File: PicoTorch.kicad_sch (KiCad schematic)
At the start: 44 parts, among them J1 Screw_Terminal_01x02, M1 Fan, M2 Fan, M3 Fan, M4 Fan, Q1 IRLB8721, Q2 IRLB8721, Q3 IRLB8721, Q4 IRLB8721, T1R1 4.7k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

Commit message: changes
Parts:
- D1, D3, D5, D7: footprint LED_THT:LED_D5.0mm_IRGrey -> LED_THT:LED_D1.8mm_W3.3mm_H2.4mm; LCSC C84256 -> (none); MPN 17-215SURC/S530-A2/TR8 -> (none); SKU 304090046 -> (none)
- J1, M4: footprint TerminalBlock_Philmore:TerminalBlock_Philmore_TB132_1x02_P5.00mm_Horizontal -> TerminalBlock_Phoenix:TerminalBlock_Phoenix_MKDS-1,5-2_1x02_P5.00mm_Horizontal
- R1, R10, R11, R12, R2, R3, R4, R5, R6, R7, R8, R9, T1R1, T1R2, T1R3, T1R4: footprint Resistor_THT:R_Axial_DIN0204_L3.6mm_D1.6mm_P5.08mm_Horizontal -> Resistor_THT:R_Axial_DIN0207_L6.3mm_D2.5mm_P2.54mm_Vertical
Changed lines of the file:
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@@
       (effects (font (size 1.27 1.27)) (justify right))
     )
-    (property "Footprint" "LED_THT:LED_D5.0mm_IRGrey" (at 74.93 33.909 0)
-      (effects (font (size 1.27 1.27)) hide)
-    )
-    (property "Datasheet" "https://www.prtice.info/IMG/pdf/CQY99.pdf" (at 70.485 32.639 0)
-      (effects (font (size 1.27 1.27)) hide)
-    )
-    (property "LCSC" "C84256" (at 70.485 33.909 90)
-      (effects (font (size 1.27 1.27)) hide)
-    )
-    (property "MPN" "17-215SURC/S530-A2/TR8 " (at 70.0532 34.8996 0)
-      (effects (font (size 1.27 1.27)) hide)
-    )
-    (property "SKU" "304090046" (at 70.0532 34.8996 0)
+    (property "Footprint" "LED_THT:LED_D1.8mm_W3.3mm_H2.4mm" (at 74.93 33.909 0)
+      (effects (font (size 1.27 1.27)) hide)
+    )
+    (property "Datasheet" "" (at 70.485 32.639 0)
       (effects (font (size 1.27 1.27)) hide)
     )
@@
       (effects (font (size 1.27 1.27)) (justify right))
     )
-    (property "Footprint" "Resistor_THT:R_Axial_DIN0204_L3.6mm_D1.6mm_P5.08mm_Horizontal" (at 130.683 37.084 0)
+    (property "Footprint" "Resistor_THT:R_Axial_DIN0207_L6.3mm_D2.5mm_P2.54mm_Vertical" (at 130.683 37.084 0)
       (effects (font (size 1.27 1.27)) hide)
     )
@@
       (effects (font (size 1.27 1.27)))
     )
-    (property "Footprint" "TerminalBlock_Philmore:TerminalBlock_Philmore_TB132_1x02_P5.00mm_Horizontal" (at 71.12 103.505 0)
+    (property "Footprint" "TerminalBlock_Phoenix:TerminalBlock_Phoenix_MKDS-1,5-2_1x02_P5.00mm_Horizontal" (at 71.12 103.505 0)
       (effects (font (size 1.27 1.27)) hide)
     )
@@
       (effects (font (size 1.27 1.27)) (justify right))
     )
-    (property "Footprint" "Resistor_THT:R_Axial_DIN0204_L3.6mm_D1.6mm_P5.08mm_Horizontal" (at 76.962 77.47 0)
+    (property "Footprint" "Resistor_THT:R_Axial_DIN0207_L6.3mm_D2.5mm_P2.54mm_Vertical" (at 76.962 77.47 0)
       (effects (font (size 1.27 1.27)) hide)
     )
@@
       (effects (font (size 1.27 1.27)) (justify right))
     )
-    (property "Footprint" "LED_THT:LED_D5.0mm_IRGrey" (at 116.586 34.163 0)
-      (effects (font (size 1.27 1.27)) hide)
-    )
-    (property "Datasheet" "https://www.prtice.info/IMG/pdf/CQY99.pdf" (at 112.141 32.893 0)
-      (effects (font (size 1.27 1.27)) hide)
-    )
-    (property "LCSC" "C84256" (at 112.141 34.163 90)
-      (effects (font (size 1.27 1.27)) hide)
-    )
-    (property "MPN" "17-215SURC/S530-A2/TR8 " (at 111.7092 35.1536 0)
-      (effects (font (size 1.27 1.27)) hide)
-    )
-    (property "SKU" "304090046" (at 111.7092 35.1536 0)
+    (property "Footprint" "LED_THT:LED_D1.8mm_W3.3mm_H2.4mm" (at 116.586 34.163 0)
+      (effects (font (size 1.27 1.27)) hide)
+    )
+    (property "Datasheet" "" (at 112.141 32.893 0)
       (effects (font (size 1.27 1.27)) hide)
     )
@@
       (effects (font (size 1.27 1.27)) (justify right))
     )
-    (property "Footprint" "Resistor_THT:R_Axial_DIN0204_L3.6mm_D1.6mm_P5.08mm_Horizontal" (at 77.47 41.148 0)
+    (property "Footprint" "Resistor_THT:R_Axial_DIN0207_L6.3mm_D2.5mm_P2.54mm_Vertical" (at 77.47 41.148 0)
       (effects (font (size 1.27 1.27)) hide)
     )
@@
       (effects (font (size 1.27 1.27)))
     )
-    (property "Footprint" "Resistor_THT:R_Axial_DIN0204_L3.6mm_D1.6mm_P5.08mm_Horizontal" (at 245.745 34.925 0)
+    (property "Footprint" "Resistor_THT:R_Axial_DIN0207_L6.3mm_D2.5mm_P2.54mm_Vertical" (at 245.745 34.925 0)
       (effects (font (size 1.27 1.27)) hide)
     )
@@
       (effects (font (size 1.27 1.27)) (justify right))
     )
-    (property "Footprint" "LED_THT:LED_D5.0mm_IRGrey" (at 116.078 70.485 0)
-      (effects (font (size 1.27 1.27)) hide)
-    )
-    (property "Datasheet" "https://www.prtice.info/IMG/pdf/CQY99.pdf" (at 111.633 69.215 0)
-      (effects (font (size 1.27 1.27)) hide)
-    )
-    (property "LCSC" "C84256" (at 111.633 70.485 90)
-      (effects (font (size 1.27 1.27)) hide)
-    )
-    (property "MPN" "17-215SURC/S530-A2/TR8 " (at 111.2012 71.4756 0)
-      (effects (font (size 1.27 1.27)) hide)
-    )
-    (property "SKU" "304090046" (at 111.2012 71.4756 0)
+    (property "Footprint" "LED_THT:LED_D1.8mm_W3.3mm_H2.4mm" (at 116.078 70.485 0)
+      (effects (font (size 1.27 1.27)) hide)
+    )
+    (property "Datasheet" "" (at 111.633 69.215 0)
       (effects (font (size 1.27 1.27)) hide)
     )
@@
       (effects (font (size 1.27 1.27)))
     )
-    (property "Footprint" "Resistor_THT:R_Axial_DIN0204_L3.6mm_D1.6mm_P5.08mm_Horizontal" (at 246.38 69.215 0)
+    (property "Footprint" "Resistor_THT:R_Axial_DIN0207_L6.3mm_D2.5mm_P2.54mm_Vertical" (at 246.38 69.215 0)
       (effects (font (size 1.27 1.27)) hide)
     )
@@
       (effects (font (size 1.27 1.27)))
     )
-    (property "Footprint" "TerminalBlock_Philmore:TerminalBlock_Philmore_TB132_1x02_P5.00mm_Horizontal" (at 35.052 74.295 0)
+    (property "Footprint" "TerminalBlock_Phoenix:TerminalBlock_Phoenix_MKDS-1,5-2_1x02_P5.00mm_Horizontal" (at 35.052 74.295 0)
       (effects (font (size 1.27 1.27)) hide)
     )
@@
       (effects (font (size 1.27 1.27)) (justify right))
     )
-    (property "Footprint" "Resistor_THT:R_Axial_DIN0204_L3.6mm_D1.6mm_P5.08mm_Horizontal" (at 88.519 73.152 0)
+    (property "Footprint" "Resistor_THT:R_Axial_DIN0207_L6.3mm_D2.5mm_P2.54mm_Vertical" (at 88.519 73.152 0)
       (effects (font (size 1.27 1.27)) hide)
     )
@@
       (effects (font (size 1.27 1.27)))
     )
-    (property "Footprint" "Resistor_THT:R_Axial_DIN0204_L3.6mm_D1.6mm_P5.08mm_Horizontal" (at 197.485 33.02 0)
+    (property "Footprint" "Resistor_THT:R_Axial_DIN0207_L6.3mm_D2.5mm_P2.54mm_Vertical" (at 197.485 33.02 0)
       (effects (font (size 1.27 1.27)) hide)
     )
@@
       (effects (font (size 1.27 1.27)) (justify right))
     )
-    (property "Footprint" "Resistor_THT:R_Axial_DIN0204_L3.6mm_D1.6mm_P5.08mm_Horizontal" (at 119.126 41.402 0)
+    (property "Footprint" "Resistor_THT:R_Axial_DIN0207_L6.3mm_D2.5mm_P2.54mm_Vertical" (at 119.126 41.402 0)
       (effects (font (size 1.27 1.27)) hide)
     )
@@
       (effects (font (size 1.27 1.27)) (justify right))
     )
-    (property "Footprint" "Resistor_THT:R_Axial_DIN0204_L3.6mm_D1.6mm_P5.08mm_Horizontal" (at 89.027 36.83 0)
+    (property "Footprint" "Resistor_THT:R_Axial_DIN0207_L6.3mm_D2.5mm_P2.54mm_Vertical" (at 89.027 36.83 0)
       (effects (font (size 1.27 1.27)) hide)
     )
@@
       (effects (font (size 1.27 1.27)) (justify right))
     )
-    (property "Footprint" "LED_THT:LED_D5.0mm_IRGrey" (at 74.422 70.231 0)
-      (effects (font (size 1.27 1.27)) hide)
-    )
-    (property "Datasheet" "https://www.prtice.info/IMG/pdf/CQY99.pdf" (at 69.977 68.961 0)
-      (effects (font (size 1.27 1.27)) hide)
-    )
-    (property "LCSC" "C84256" (at 69.977 70.231 90)
-      (effects (font (size 1.27 1.27)) hide)
-    )
-    (property "MPN" "17-215SURC/S530-A2/TR8 " (at 69.5452 71.2216 0)
-      (effects (font (size 1.27 1.27)) hide)
-    )
-    (property "SKU" "304090046" (at 69.5452 71.2216 0)
+    (property "Footprint" "LED_THT:LED_D1.8mm_W3.3mm_H2.4mm" (at 74.422 70.231 0)
+      (effects (font (size 1.27 1.27)) hide)
+    )
+    (property "Datasheet" "" (at 69.977 68.961 0)
       (effects (font (size 1.27 1.27)) hide)
     )
@@
       (effects (font (size 1.27 1.27)) (justify right))
     )
-    (property "Footprint" "Resistor_THT:R_Axial_DIN0204_L3.6mm_D1.6mm_P5.08mm_Horizontal" (at 70.485 42.799 0)
+    (property "Footprint" "Resistor_THT:R_Axial_DIN0207_L6.3mm_D2.5mm_P2.54mm_Vertical" (at 70.485 42.799 0)
       (effects (font (size 1.27 1.27)) hide)
     )
@@
       (effects (font (size 1.27 1.27)) (justify right))
     )
-    (property "Footprint" "Resistor_THT:R_Axial_DIN0204_L3.6mm_D1.6mm_P5.08mm_Horizontal" (at 111.633 79.375 0)
+    (property "Footprint" "Resistor_THT:R_Axial_DIN0207_L6.3mm_D2.5mm_P2.54mm_Vertical" (at 111.633 79.375 0)
       (effects (font (size 1.27 1.27)) hide)
     )
@@
       (effects (font (size 1.27 1.27)) (justify right))
     )
-    (property "Footprint" "Resistor_THT:R_Axial_DIN0204_L3.6mm_D1.6mm_P5.08mm_Horizontal" (at 118.618 77.724 0)
+    (property "Footprint" "Resistor_THT:R_Axial_DIN0207_L6.3mm_D2.5mm_P2.54mm_Vertical" (at 118.618 77.724 0)
       (effects (font (size 1.27 1.27)) hide)
     )
@@
       (effects (font (size 1.27 1.27)))
     )
-    (property "Footprint" "Resistor_THT:R_Axial_DIN0204_L3.6mm_D1.6mm_P5.08mm_Horizontal" (at 199.39 67.31 0)
+    (property "Footprint" "Resistor_THT:R_Axial_DIN0207_L6.3mm_D2.5mm_P2.54mm_Vertical" (at 199.39 67.31 0)
       (effects (font (size 1.27 1.27)) hide)
     )
@@
       (effects (font (size 1.27 1.27)) (justify right))
     )
-    (property "Footprint" "Resistor_THT:R_Axial_DIN0204_L3.6mm_D1.6mm_P5.08mm_Horizontal" (at 69.977 79.121 0)
+    (property "Footprint" "Resistor_THT:R_Axial_DIN0207_L6.3mm_D2.5mm_P2.54mm_Vertical" (at 69.977 79.121 0)
       (effects (font (size 1.27 1.27)) hide)
     )
@@
       (effects (font (size 1.27 1.27)) (justify right))
     )
-    (property "Footprint" "Resistor_THT:R_Axial_DIN0204_L3.6mm_D1.6mm_P5.08mm_Horizontal" (at 130.175 73.406 0)
+    (property "Footprint" "Resistor_THT:R_Axial_DIN0207_L6.3mm_D2.5mm_P2.54mm_Vertical" (at 130.175 73.406 0)
       (effects (font (size 1.27 1.27)) hide)
     )
@@
       (effects (font (size 1.27 1.27)) (justify right))
     )
-    (property "Footprint" "Resistor_THT:R_Axial_DIN0204_L3.6mm_D1.6mm_P5.08mm_Horizontal" (at 112.141 43.053 0)
-      (effects (font (size 1.27 1.27)) hide)
-    )
+    (property "Footprint" "Resistor_THT:R_Axial_DIN0207_L6.3mm_D2.5mm_P2.54mm_Vertical" (at 112.141 43.053 0)
+      (effects (font (size 1.27 1.27)) hide)
+    )

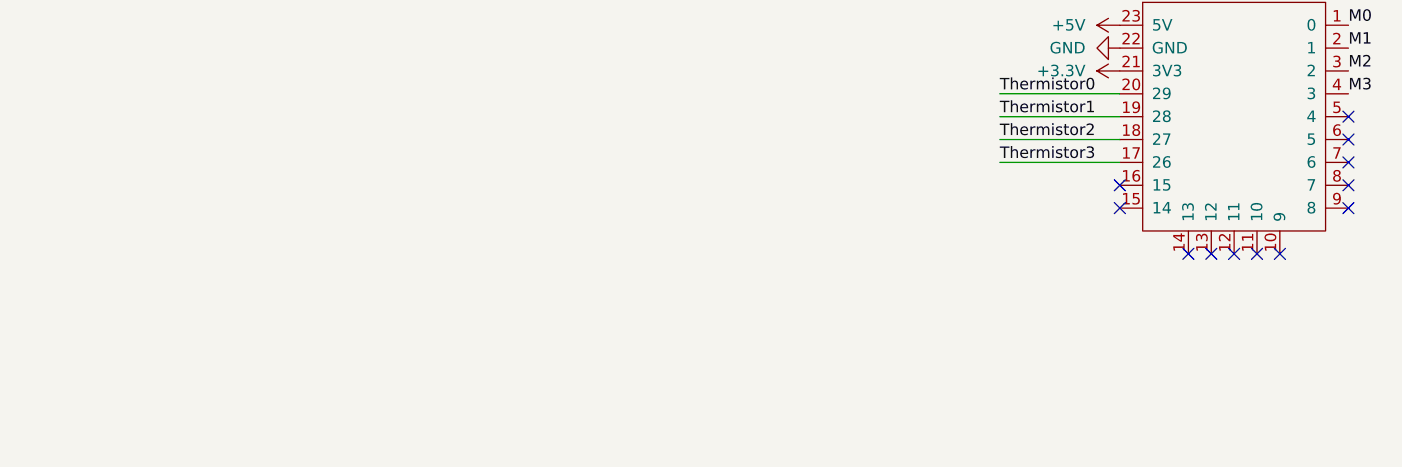
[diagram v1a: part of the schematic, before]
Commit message: feat: First untested release
This has not been tested. It passes ERC and DRC, but zero actual
physical testing of this board has been done. It needs to be ordered
and tested to completion, as well as documenting amp limits of the
board. Please reach out if you have done any testing.
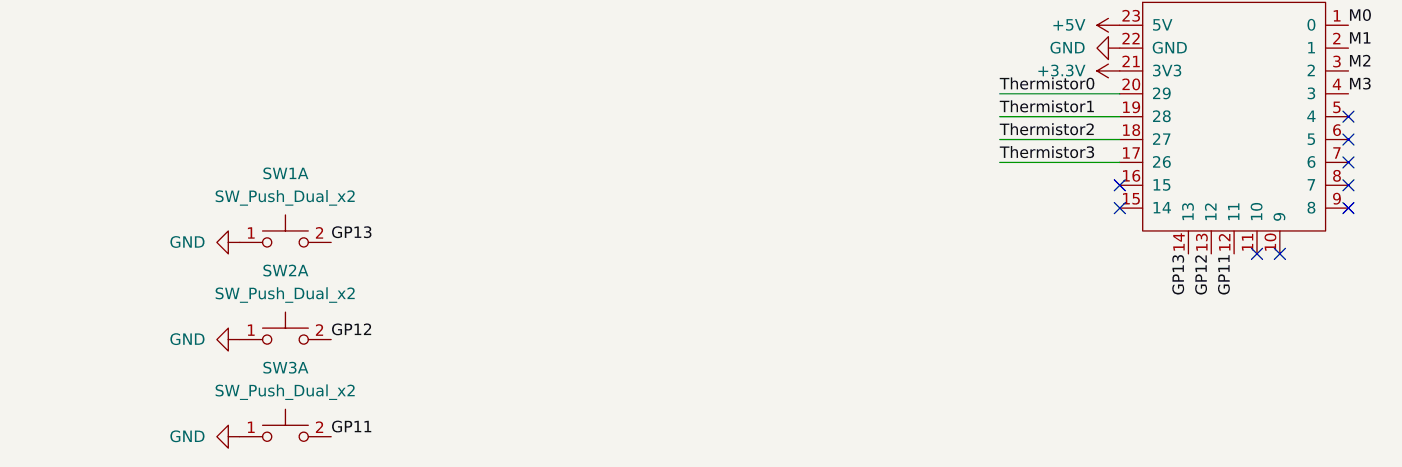
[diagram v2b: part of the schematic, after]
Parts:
- added SW1, SW2, SW3: SW_Push_Dual_x2, Connector_JST:JST_XH_B2B-XH-A_1x02_P2.50mm_Vertical, symbol Switch:SW_Push_Dual_x2
- D2, D4, D6, D8: footprint Diode_THT:D_DO-201AD_P12.70mm_Horizontal -> Diode_THT:D_DO-34_SOD68_P7.62mm_Horizontal
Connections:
- net GND: now also SW1.1 (C), SW2.1 (C), SW3.1 (C)
- net GP11: now reaches ZERO1.12 (11)
- net GP11: now also SW3.2 (D)
- net GP12: now reaches ZERO1.13 (12)
- net GP12: now also SW2.2 (D)
- net GP13: now reaches ZERO1.14 (13)
- net GP13: now also SW1.2 (D)
- no-connect marks 12 -> 9
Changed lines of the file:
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@@
   (no_connect (at 187.96 128.27))
   (no_connect (at 187.96 130.81))
-  (no_connect (at 170.18 140.97))
-  (no_connect (at 175.26 140.97))
   (no_connect (at 162.56 133.35))
   (no_connect (at 187.96 125.73))
   (no_connect (at 180.34 140.97))
-  (no_connect (at 172.72 140.97))
   (no_connect (at 162.56 135.89))
   (wire (pts (xy 76.962 71.12) (xy 81.407 71.12))
@@
     (effects (font (size 1.27 1.27)) (justify left bottom))
   )
+  (label "GP11" (at 74.93 161.29 0) (fields_autoplaced)
+    (effects (font (size 1.27 1.27)) (justify left bottom))
+  )
   (label "Thermistor0" (at 149.225 123.19 0) (fields_autoplaced)
     (effects (font (size 1.27 1.27)) (justify left bottom))
@@
     (effects (font (size 1.27 1.27)) (justify left bottom))
   )
+  (label "GP12" (at 172.72 140.97 270) (fields_autoplaced)
+    (effects (font (size 1.27 1.27)) (justify right bottom))
+  )
+  (label "GP11" (at 175.26 140.97 270) (fields_autoplaced)
+    (effects (font (size 1.27 1.27)) (justify right bottom))
+  )
   (label "Mosfet2" (at 61.087 65.151 0) (fields_autoplaced)
     (effects (font (size 1.27 1.27)) (justify left bottom))
@@
     (effects (font (size 1.27 1.27)) (justify left bottom))
   )
+  (label "GP12" (at 74.93 150.495 0) (fields_autoplaced)
+    (effects (font (size 1.27 1.27)) (justify left bottom))
+  )
   (label "Thermistor3" (at 149.225 130.81 0) (fields_autoplaced)
     (effects (font (size 1.27 1.27)) (justify left bottom))
@@
     (effects (font (size 1.27 1.27)) (justify left bottom))
   )
+  (label "GP13" (at 170.18 140.97 270) (fields_autoplaced)
+    (effects (font (size 1.27 1.27)) (justify right bottom))
+  )
   (label "Thermistor3" (at 252.73 86.36 0) (fields_autoplaced)
+    (effects (font (size 1.27 1.27)) (justify left bottom))
+  )
+  (label "GP13" (at 74.93 139.7 0) (fields_autoplaced)
     (effects (font (size 1.27 1.27)) (justify left bottom))
   )
@@
     )
   )
+  (symbol (lib_id "power:GND") (at 64.77 161.29 270) (unit 1)
+    (in_bom yes) (on_board yes) (dnp no) (fields_autoplaced)
+    (property "Reference" "#PWR011" (at 58.42 161.29 0)
+      (effects (font (size 1.27 1.27)) hide)
+    )
+    (property "Value" "GND" (at 60.96 161.29 90)
+      (effects (font (size 1.27 1.27)) (justify right))
+    )
+    (property "Footprint" "" (at 64.77 161.29 0)
+      (effects (font (size 1.27 1.27)) hide)
+    )
+    (property "Datasheet" "" (at 64.77 161.29 0)
+      (effects (font (size 1.27 1.27)) hide)
+    )
+    (pin "1")
+    (instances
+      (project "PicoTorch"
+        (path "/3ca3dbff-3760-4281-b935-18bad2d2e060"
+          (reference "#PWR011") (unit 1)
+        )
+      )
+    )
+  )
   (symbol (lib_id "LED:CQY99") (at 70.485 33.909 270) (unit 1)
     (in_bom yes) (on_board yes) (dnp no)
@@
     )
   )
+  (symbol (lib_id "Switch:SW_Push_Dual_x2") (at 69.85 161.29 0) (unit 1)
+    (in_bom yes) (on_board yes) (dnp no) (fields_autoplaced)
+    (property "Reference" "SW3" (at 69.85 153.67 0)
+      (effects (font (size 1.27 1.27)))
+    )
+    (property "Value" "SW_Push_Dual_x2" (at 69.85 156.21 0)
+      (effects (font (size 1.27 1.27)))
+    )
+    (property "Footprint" "Connector_JST:JST_XH_B2B-XH-A_1x02_P2.50mm_Vertical" (at 69.85 156.21 0)
+      (effects (font (size 1.27 1.27)) hide)
+    )
+    (property "Datasheet" "~" (at 69.85 156.21 0)
+      (effects (font (size 1.27 1.27)) hide)
+    )
+    (pin "1")
+    (pin "2")
+    (pin "3")
+    (pin "4")
+    (instances
+      (project "PicoTorch"
+        (path "/3ca3dbff-3760-4281-b935-18bad2d2e060"
+          (reference "SW3") (unit 1)
+        )
+      )
+    )
+  )
   (symbol (lib_id "Device:D_Zener") (at 76.2 59.309 0) (unit 1)
     (in_bom yes) (on_board yes) (dnp no) (fields_autoplaced)
@@
       (effects (font (size 1.27 1.27)))
     )
-    (property "Footprint" "Diode_THT:D_DO-201AD_P12.70mm_Horizontal" (at 76.2 59.309 0)
+    (property "Footprint" "Diode_THT:D_DO-34_SOD68_P7.62mm_Horizontal" (at 76.2 59.309 0)
       (effects (font (size 1.27 1.27)) hide)
     )
@@
         (path "/3ca3dbff-3760-4281-b935-18bad2d2e060"
           (reference "J1") (unit 1)
+        )
+      )
+    )
+  )
+  (symbol (lib_id "Switch:SW_Push_Dual_x2") (at 69.85 139.7 0) (unit 1)
+    (in_bom yes) (on_board yes) (dnp no) (fields_autoplaced)
+    (property "Reference" "SW1" (at 69.85 132.08 0)
+      (effects (font (size 1.27 1.27)))
+    )
+    (property "Value" "SW_Push_Dual_x2" (at 69.85 134.62 0)
+      (effects (font (size 1.27 1.27)))
+    )
+    (property "Footprint" "Connector_JST:JST_XH_B2B-XH-A_1x02_P2.50mm_Vertical" (at 69.85 134.62 0)
+      (effects (font (size 1.27 1.27)) hide)
+    )
+    (property "Datasheet" "~" (at 69.85 134.62 0)
+      (effects (font (size 1.27 1.27)) hide)
+    )
+    (pin "1")
+    (pin "2")
+    (pin "3")
+    (pin "4")
+    (instances
+      (project "PicoTorch"
+        (path "/3ca3dbff-3760-4281-b935-18bad2d2e060"
+          (reference "SW1") (unit 1)
         )
       )
@@
       (effects (font (size 1.27 1.27)))
     )
-    (property "Footprint" "Diode_THT:D_DO-201AD_P12.70mm_Horizontal" (at 76.327 22.987 0)
+    (property "Footprint" "Diode_THT:D_DO-34_SOD68_P7.62mm_Horizontal" (at 76.327 22.987 0)
       (effects (font (size 1.27 1.27)) hide)
     )
@@
       (effects (font (size 1.27 1.27)))
     )
-    (property "Footprint" "Diode_THT:D_DO-201AD_P12.70mm_Horizontal" (at 118.364 58.928 0)
+    (property "Footprint" "Diode_THT:D_DO-34_SOD68_P7.62mm_Horizontal" (at 118.364 58.928 0)
       (effects (font (size 1.27 1.27)) hide)
     )
@@
       (effects (font (size 1.27 1.27)))
     )
-    (property "Footprint" "Diode_THT:D_DO-201AD_P12.70mm_Horizontal" (at 117.729 22.86 0)
+    (property "Footprint" "Diode_THT:D_DO-34_SOD68_P7.62mm_Horizontal" (at 117.729 22.86 0)
       (effects (font (size 1.27 1.27)) hide)
     )
@@
     )
   )
+  (symbol (lib_id "Switch:SW_Push_Dual_x2") (at 69.85 150.495 0) (unit 1)
+    (in_bom yes) (on_board yes) (dnp no) (fields_autoplaced)
+    (property "Reference" "SW2" (at 69.85 142.875 0)
+      (effects (font (size 1.27 1.27)))
+    )
+    (property "Value" "SW_Push_Dual_x2" (at 69.85 145.415 0)
+      (effects (font (size 1.27 1.27)))
+    )
+    (property "Footprint" "Connector_JST:JST_XH_B2B-XH-A_1x02_P2.50mm_Vertical" (at 69.85 145.415 0)
+      (effects (font (size 1.27 1.27)) hide)
+    )
+    (property "Datasheet" "~" (at 69.85 145.415 0)
+      (effects (font (size 1.27 1.27)) hide)
+    )
+    (pin "1")
+    (pin "2")
+    (pin "3")
+    (pin "4")
+    (instances
+      (project "PicoTorch"
+        (path "/3ca3dbff-3760-4281-b935-18bad2d2e060"
+          (reference "SW2") (unit 1)
+        )
+      )
+    )
+  )
   (symbol (lib_id "Device:Thermistor_NTC") (at 214.63 33.02 90) (unit 1)
     (in_bom yes) (on_board yes) (dnp no) (fields_autoplaced)
@@
     )
   )
+  (symbol (lib_id "power:GND") (at 64.77 150.495 270) (unit 1)
+    (in_bom yes) (on_board yes) (dnp no) (fields_autoplaced)
+    (property "Reference" "#PWR010" (at 58.42 150.495 0)
+      (effects (font (size 1.27 1.27)) hide)
+    )
+    (property "Value" "GND" (at 60.96 150.495 90)
+      (effects (font (size 1.27 1.27)) (justify right))
+    )
+    (property "Footprint" "" (at 64.77 150.495 0)
+      (effects (font (size 1.27 1.27)) hide)
+    )
+    (property "Datasheet" "" (at 64.77 150.495 0)
+      (effects (font (size 1.27 1.27)) hide)
+    )
+    (pin "1")
+    (instances
+      (project "PicoTorch"
+        (path "/3ca3dbff-3760-4281-b935-18bad2d2e060"
+          (reference "#PWR010") (unit 1)
+        )
+      )
+    )
+  )
   (symbol (lib_id "pspice:R") (at 119.126 41.402 0) (mirror x) (unit 1)
     (in_bom yes) (on_board yes) (dnp no)
@@
         )
       )
+    )
+  )
+  (symbol (lib_id "power:GND") (at 64.77 139.7 270) (unit 1)
+    (in_bom yes) (on_board yes) (dnp no) (fields_autoplaced)
+    (property "Reference" "#PWR09" (at 58.42 139.7 0)
+      (effects (font (size 1.27 1.27)) hide)
+    )
+    (property "Value" "GND" (at 60.96 139.7 90)
+      (effects (font (size 1.27 1.27)) (justify right))
+    )
+    (property "Footprint" "" (at 64.77 139.7 0)
+      (effects (font (size 1.27 1.27)) hide)
+    )
+    (property "Datasheet" "" (at 64.77 139.7 0)
+      (effects (font (size 1.27 1.27)) hide)
+    )
+    (pin "1")
+    (instances
+      (project "PicoTorch"
+        (path "/3ca3dbff-3760-4281-b935-18bad2d2e060"
+          (reference "#PWR09") (unit 1)
+        )
+      )
